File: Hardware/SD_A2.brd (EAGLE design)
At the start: 100.2 x 77.7 mm, 25 parts, among them IC1 74LS245N, IC2 LM317, IC4 XC9572XL, IC5 28C64ASO

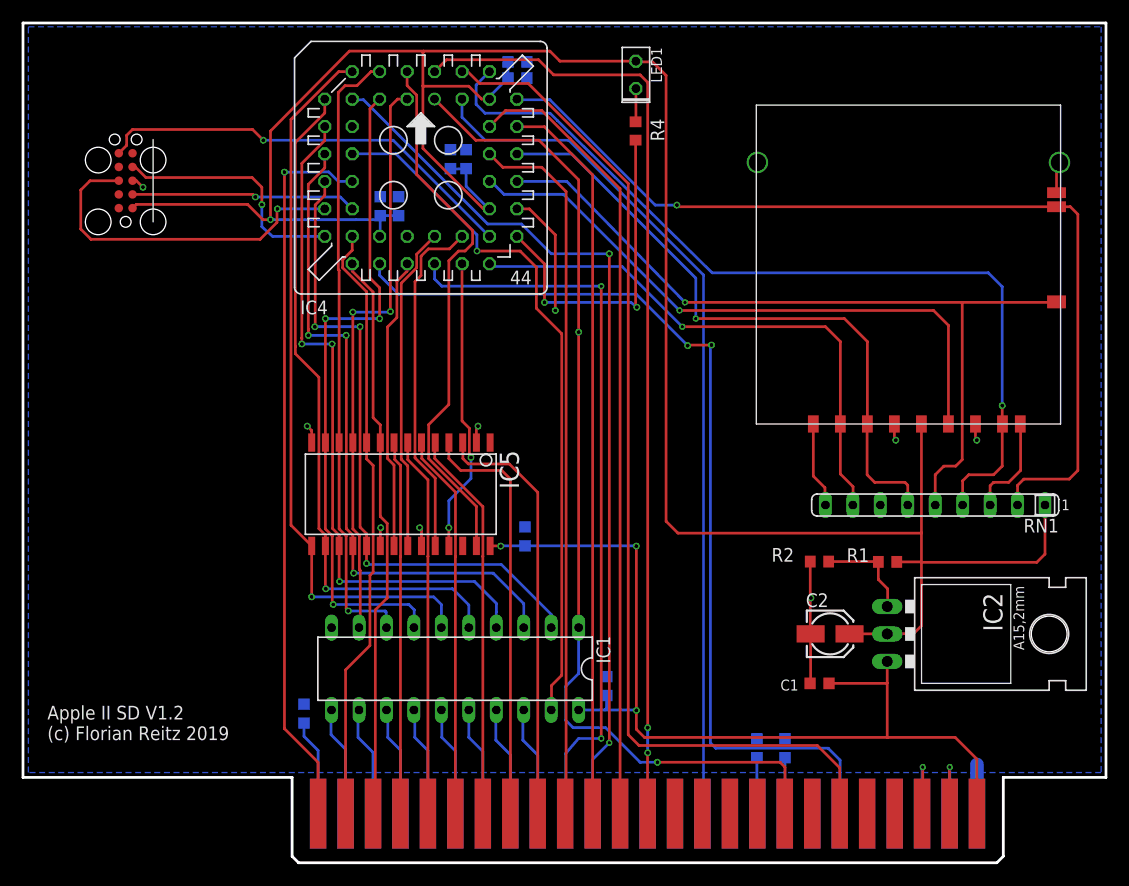
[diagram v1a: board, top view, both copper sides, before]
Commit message: CPLD changed to VQFP package
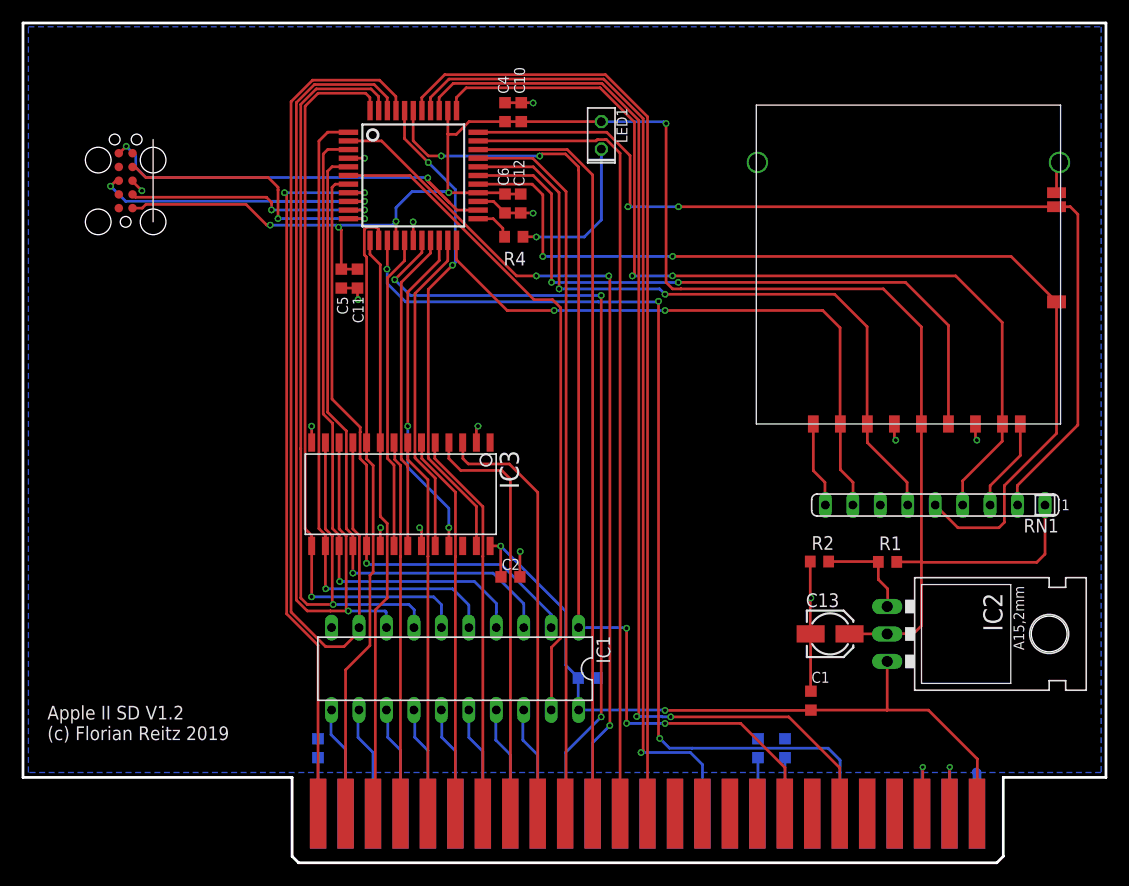
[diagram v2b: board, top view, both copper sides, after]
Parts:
- C11, C12: value 100n -> 10n
- C13: value 100n -> 1u; device rcl:C0603K -> rcl@1:153CLV-0405
- C2: value 1u -> 100n; device rcl:153CLV-0405 -> rcl:C0603K
- C8, C9: value 10n -> 100n
- IC4: device xilinx-xc9:S44 -> xilinx-xc9:SQFP-S-10X10-44
- moved C8 64.7 mm to (27.3, 10.5), turned to 90 degrees
- moved C9 61.6 mm to (70.5, 10.5)
- moved C7 60.8 mm to (68.0, 10.5)
- moved C12 56.0 mm to (46.0, 60.9), flipped to the top, turned to 270 degrees
- moved C4 53.9 mm to (44.6, 69.3), flipped to the top
- moved C11 40.6 mm to (30.9, 54.0), flipped to the top, turned to 270 degrees
- moved C2 30.0 mm to (45.1, 26.4)
- moved C5 25.8 mm to (29.4, 54.0), flipped to the top, turned to 270 degrees
- moved R4 14.9 mm to (45.4, 57.8), turned to 180 degrees
- moved C3 14.3 mm to (52.2, 17.0), turned to 180 degrees
- moved C13 12.6 mm to (74.7, 21.1), flipped to the top, turned to 0 degrees
- moved C6 11.6 mm to (44.6, 60.9), flipped to the top, turned to 270 degrees
- moved C10 7.86 mm to (46.1, 69.3), flipped to the top
- moved LED1 6.45 mm to (53.5, 67.2)
- moved C1 1.79 mm to (72.9, 14.9), turned to 90 degrees
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- renumbered IC5 to IC3
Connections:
- net !CS: now also IC4.22; no longer IC4.28
- net !DEV_SEL: now also IC4.18; no longer IC4.24
- net !G: now also IC4.6; no longer IC4.12
- net !IO_SEL: now also IC4.8; no longer IC4.14
- net !IO_STR: now also IC4.36; no longer IC4.42
- net !LED: now also IC4.23; no longer IC4.29
- net !OE: now also IC4.19; no longer IC4.25
- net !RESET: now also IC4.14; no longer IC4.20
- net !WE: now also IC4.40; no longer IC4.2
- net +12V: now also C8.1; no longer C11.1
- net +3V3: now also C11.1, C12.1, C13.+, C4.1, IC4.15, IC4.26, IC4.35; no longer C2.+, C7.1, C8.1, C9.1, IC4.21, IC4.32, IC4.41
- net +5V: now also C2.1; no longer C4.1
- net -12V: now also C9.1; no longer C12.1
- net -5V: now also C7.1; no longer C13.1
- net 7M: now also IC4.37; no longer IC4.43
- net ADD0: now also IC4.13; no longer IC4.19
- net ADD1: now also IC4.12; no longer IC4.18
- net ADD10: now also IC4.32; no longer IC4.38
- net ADD11: now also IC4.38; no longer IC4.44
- net ADD8: now also IC4.30; no longer IC4.36
- net ADD9: now also IC4.31; no longer IC4.37
- net B10: now also IC4.16; no longer IC4.22
- net B8: now also IC4.20; no longer IC4.26
- net B9: now also IC4.21; no longer IC4.27
- net CARD: now also IC4.27; no longer IC4.33
- net CLK: now also IC4.28; no longer IC4.34
- net DATA0: now also IC4.41; no longer IC4.3
- net DATA1: now also IC4.42; no longer IC4.4
- net DATA2: now also IC4.43; no longer IC4.5
- net DATA3: now also IC4.44; no longer IC4.6
- net DATA4: now also IC4.1; no longer IC4.7
- net DATA5: now also IC4.3; no longer IC4.9
- net DATA6: now also IC4.5; no longer IC4.11
- net DATA7: now also IC4.7; no longer IC4.13
- net GND: now also C13.-, C2.2, IC4.17, IC4.25, IC4.4; no longer C13.2, C2.-, IC4.10, IC4.23, IC4.31
- net MISO: now also IC4.34; no longer IC4.40
- net MOSI: now also IC4.29; no longer IC4.35
- net PHI_0: now also IC4.2; no longer IC4.8
- net R/!W: now also IC4.39; no longer IC4.1
- net TCK: now also IC4.11; no longer IC4.17
- net TDI: now also IC4.9; no longer IC4.15
- net TDO: now also IC4.24; no longer IC4.30
- net TMS: now also IC4.10; no longer IC4.16
- net WP: now also IC4.33; no longer IC4.39
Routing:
- net +3V3: track 220.6 -> 168.3 mm, vias 1 -> 5
- net DATA0: track 53.8 -> 85.7 mm, vias 2 -> 0
- net !LED: track 31.4 -> 3.50 mm, vias 2 -> 0
- net DATA1: track 58.0 -> 83.1 mm
- net DATA2: track 62.2 -> 83.0 mm, vias 3 -> 1
- net +5V: track 87.4 -> 70.4 mm, vias 3 -> 2
- net CARD: track 75.1 -> 91.3 mm, vias 1 -> 2
- net 7M: track 80.1 -> 92.7 mm, vias 0 -> 1
- net N$29: track 3.08 -> 14.5 mm, vias 0 -> 1
- net !IO_STR: track 95.7 -> 102.1 mm, vias 0 -> 2
- net CLK: track 57.1 -> 63.2 mm, vias 1 -> 2
- net MISO: track 82.2 -> 88.1 mm, vias 1 -> 2
- net !CS: track 51.1 -> 56.8 mm, vias 1 -> 2
- net MOSI: track 60.1 -> 65.4 mm, vias 1 -> 2
- net !DEV_SEL: track 68.5 -> 73.7 mm, vias 2 -> 3
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
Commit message: LM317 replaced with LM1117
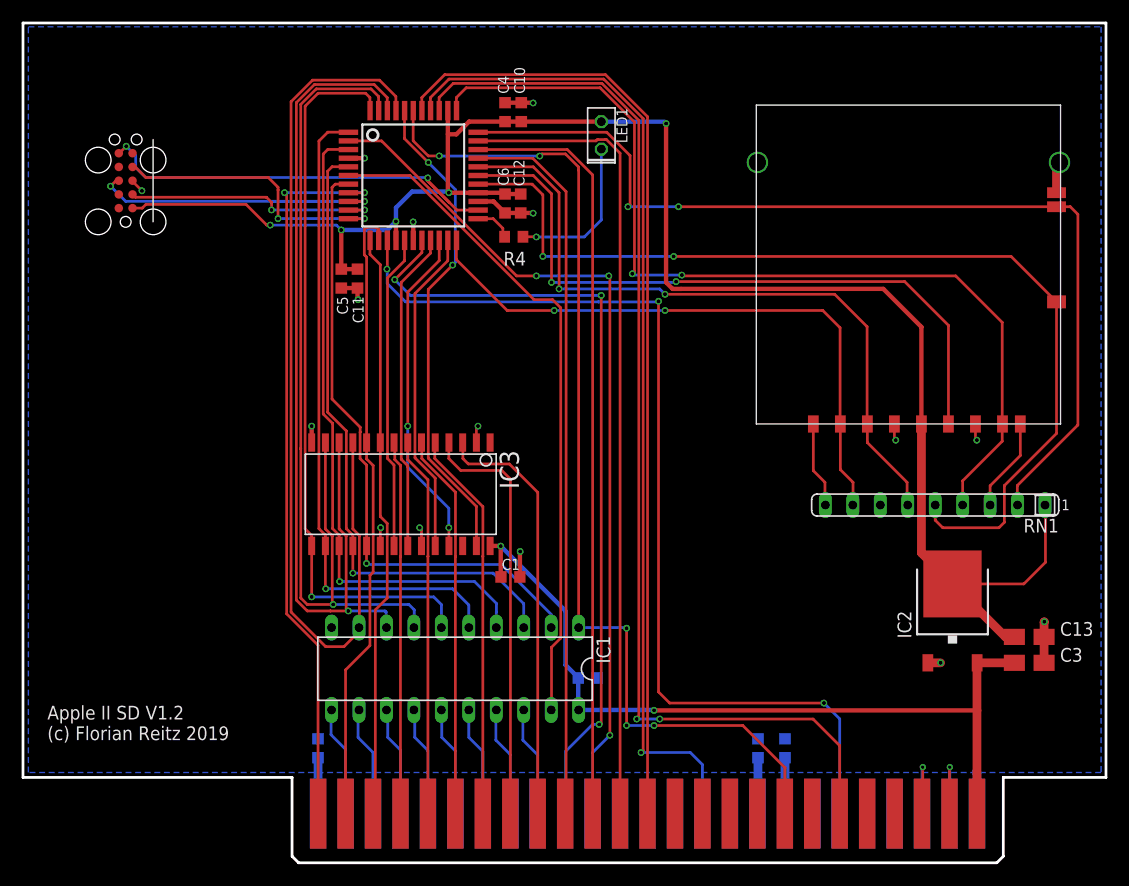
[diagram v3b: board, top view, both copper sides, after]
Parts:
- removed R1: 200, rcl:R0603
- removed R2: 330, rcl:R0603
- C13: value 1u -> 10u/16V; device rcl@1:153CLV-0405 -> rcl@1:A/3216-18R
- C3: value 100n -> 10u/16V; device rcl:C0603K -> rcl@1:A/3216-18R
- IC2: value LM317 -> LM1117DTX-3.3; device v-reg:317TL -> lm1117:TO252
- moved C3 40.9 mm to (93.1, 18.4), flipped to the top
- moved C1 30.1 mm to (45.1, 26.4), turned to 0 degrees
- moved C13 18.4 mm to (93.1, 20.8), turned to 180 degrees
- moved C2 11.8 mm to (52.2, 17.0), flipped to the bottom, turned to 180 degrees
- moved IC2 3.08 mm to (86.0, 23.2), turned to 0 degrees
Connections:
- removed net N$1: IC2.1, R1.1, R2.2
- net +3V3: now also IC2.TAB; no longer IC2.2, R1.2
- net +5V: now also C3.+, IC2.2; no longer C3.1, IC2.3
- net GND: now also C3.-, IC2.1; no longer C3.2, R2.1
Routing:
- net N$1: track 9.12 -> 0.00 mm
- net GND: track 46.1 -> 39.0 mm, vias 14 -> 15
- net +3V3: track 168.3 -> 162.3 mm
- net +5V: track 70.4 -> 76.3 mm
- net !IO_STR: track 102.1 -> 103.2 mm
- net CARD: track 91.3 -> 92.1 mm

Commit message: Gerber for V1.2
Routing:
- net GND: track 39.0 -> 42.4 mm, vias 15 -> 19
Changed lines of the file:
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@@
 <?xml version="1.0" encoding="utf-8"?>
 <!DOCTYPE eagle SYSTEM "eagle.dtd">
-<eagle version="8.2.2">
+<eagle version="7.7.0">
 <drawing>
 <settings>
@@
 <wire x1="95.625" y1="61.9" x2="95.625" y2="64.425" width="0.8128" layer="1"/>
 <wire x1="95.625" y1="64.425" x2="95.9" y2="64.7" width="0.8128" layer="1"/>
+<wire x1="44.6" y1="70.2" x2="43.6" y2="70.2" width="0.4064" layer="1"/>
+<via x="43.6" y="70.2" extent="1-16" drill="0.35"/>
+<via x="43.6" y="61" extent="1-16" drill="0.35"/>
+<via x="29.4" y="52" extent="1-16" drill="0.35"/>
+<wire x1="29.5" y1="53" x2="29.4" y2="53" width="0.4064" layer="1"/>
+<wire x1="29.4" y1="53" x2="29.4" y2="52" width="0.4064" layer="1"/>
+<via x="94.5" y="17.1" extent="1-16" drill="0.35"/>
+<wire x1="94.5" y1="18.4" x2="94.5" y2="17.1" width="0.8128" layer="1"/>
 </signal>
 <signal name="+5V">

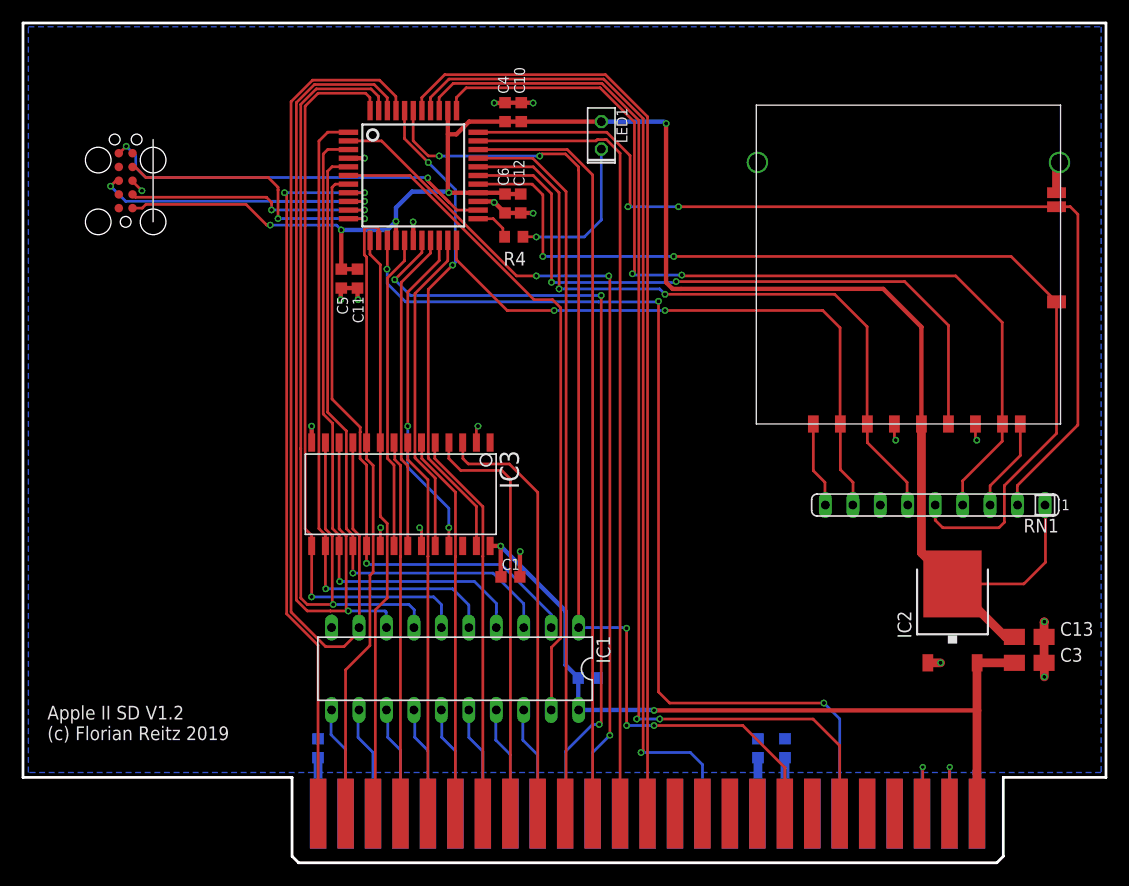
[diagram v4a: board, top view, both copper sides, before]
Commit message: Pullup on /WE added
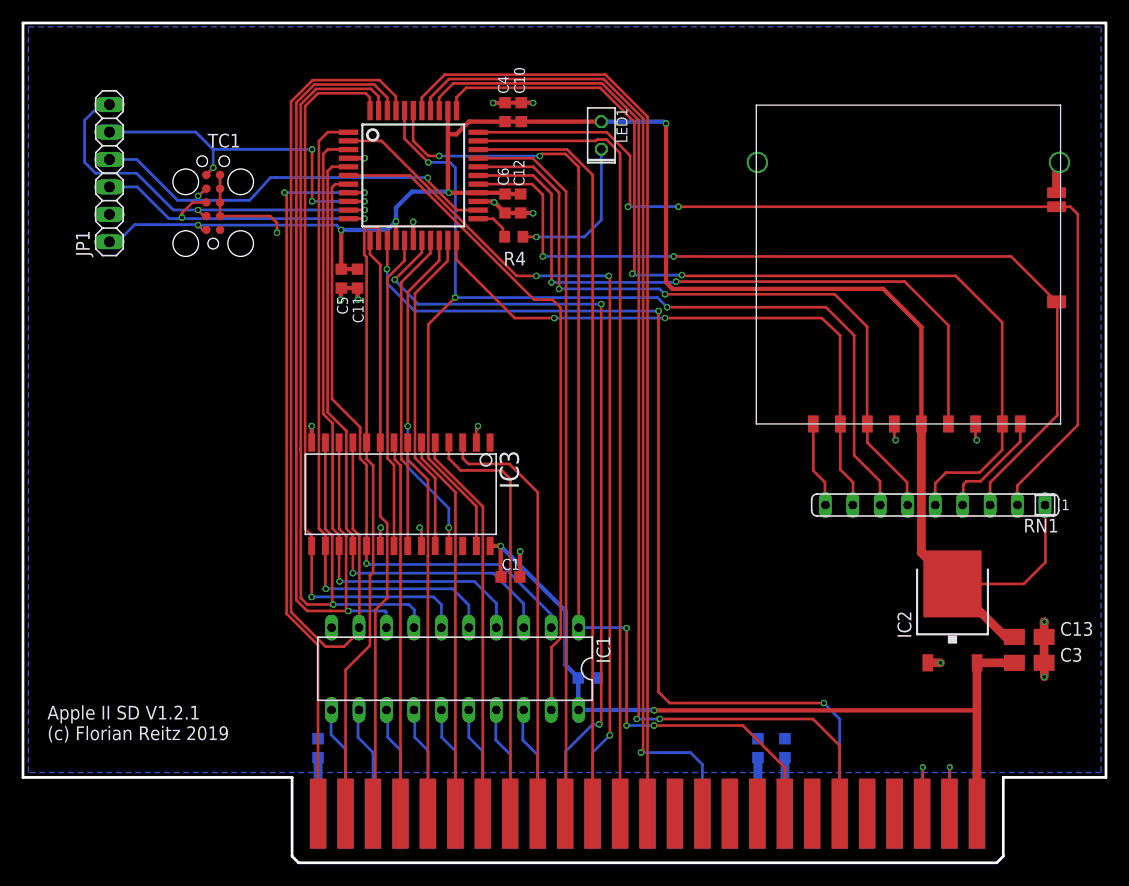
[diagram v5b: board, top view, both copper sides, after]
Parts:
- removed U$1: TC2050-NL, eagle_tag-connect-2050:TC2050-MCP
- added JP1: (no value), pinhead:1X06
- added TC1: TC2050-IDC, TagConnect:TC2050-IDC
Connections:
- removed net DAT1: RN1.3, U$2.P8
- new net N$2: RN1.4, U$2.P8
- net !WE: now also RN1.7
- net +3V3: now also JP1.1, TC1.2; no longer U$1.1
- net CARD: now also RN1.3; no longer RN1.5
- net GND: now also JP1.2, TC1.3, TC1.5, TC1.7, TC1.9; no longer U$1.3
- net MISO: now also RN1.5; no longer RN1.4
- net TCK: now also JP1.3, TC1.6; no longer U$1.4
- net TDI: now also JP1.5, TC1.10; no longer U$1.8
- net TDO: now also JP1.4, TC1.8; no longer U$1.6
- net TMS: now also JP1.6, TC1.4; no longer U$1.2
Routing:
- net !WE: track 45.8 -> 102.1 mm, vias 2 -> 3
- net TMS: track 24.0 -> 37.1 mm
- net N$2: track 0.00 -> 10.5 mm
- net CARD: track 92.1 -> 82.8 mm
- net GND: track 42.4 -> 51.5 mm
- net DAT1: track 8.69 -> 0.00 mm
- net +3V3: track 162.3 -> 165.3 mm
- net TCK: track 26.6 -> 29.6 mm
- net MISO: track 88.0 -> 90.9 mm
- net TDI: track 35.3 -> 33.2 mm, vias 2 -> 4
- net !RESET: track 92.6 -> 92.1 mm
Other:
- board text added: "Apple II SD V1.2.1 (c) Florian Reitz 2019"
- board text removed: "Apple II SD V1.2 (c) Florian Reitz 2019"

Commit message: Longer slot pins
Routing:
- net +12V: track 5.19 -> 5.95 mm
- net DMA: track 8.63 -> 9.38 mm
- net !RESET: track 92.1 -> 92.9 mm
- net INT: track 8.66 -> 9.40 mm
- net 7M: track 92.7 -> 93.4 mm
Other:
- outline, holes or cut-outs redrawn
